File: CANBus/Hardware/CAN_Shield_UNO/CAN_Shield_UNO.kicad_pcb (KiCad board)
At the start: 2 copper layers, 68.6 x 53.3 mm, 39 parts, among them J1 Power, J2 Digital/PWM, J3 Analog, J4 Digital/PWM, J7 Screw_Terminal_01x02, U2 TCAN1051HGV

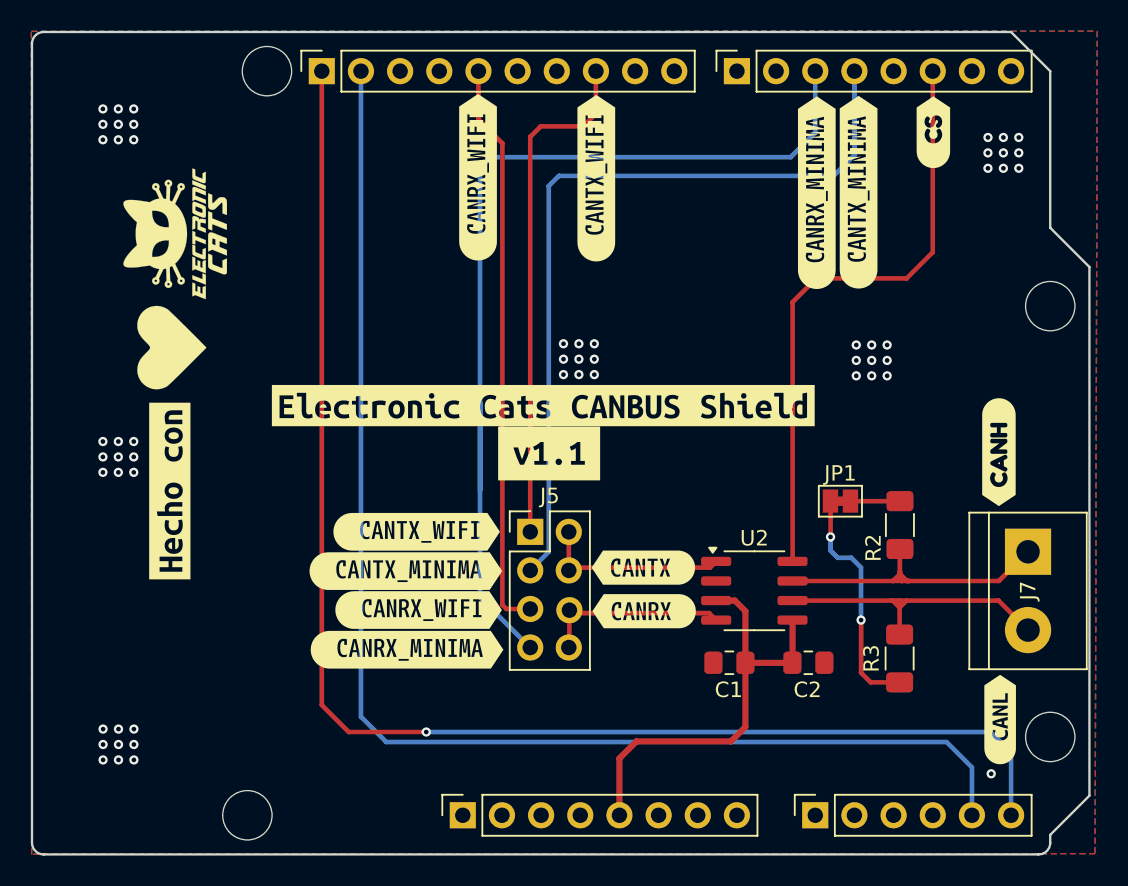
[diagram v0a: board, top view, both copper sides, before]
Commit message: feat(hw): to add hardware components
- Replacing the CAN Bus driver
- Adding a pull-down resistor to the CS pin
- Adding a 1nF capacitor to the 120 ohm terminating resistor
- Adding 2EDN7534F (54 Gate driver) channels to handle high current outputs; in addition adding a diode to power them if the board is only powered through USB
- Adding TL4050A50IDBZT (Precision micropower shunt voltage) to generate a precise 5V reference
- Adding protection diodes for A0 and A1 analog inputs
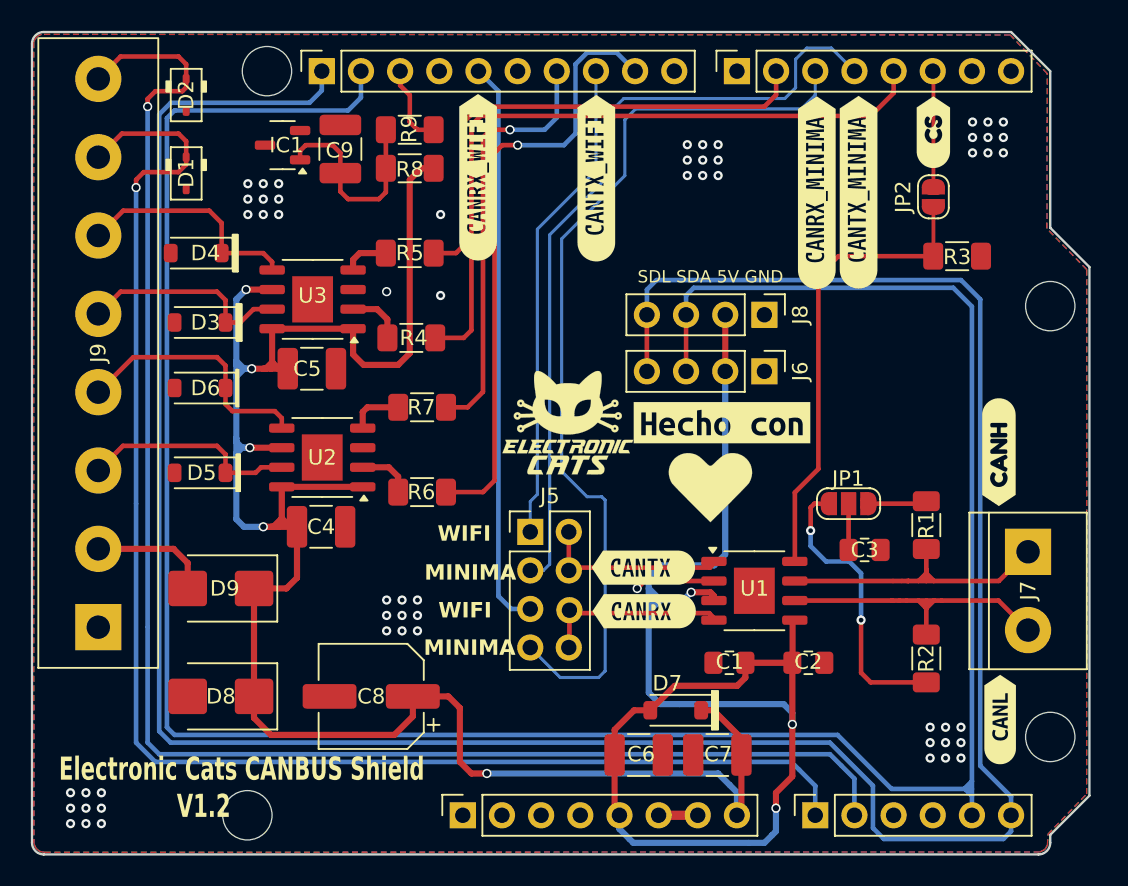
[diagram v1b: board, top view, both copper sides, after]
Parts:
- removed the kibuzzard-66182154 at (133.2, 70.9)
- removed kibuzzard-66182706: G***, kibuzzard-66182706
- removed kibuzzard-6618271B: G***, kibuzzard-6618271B
- removed kibuzzard-6618272A: G***, kibuzzard-6618272A
- removed kibuzzard-66182736: G***, kibuzzard-66182736
- removed kibuzzard-667B328E: G***, kibuzzard-667B328E
- removed kibuzzard-667B3298: G***, kibuzzard-667B3298
- added C3: 1000pF, Capacitor_SMD:C_0805_2012Metric_Pad1.18x1.45mm_HandSolder, F.Cu at (154.0, 80.2)
- added C4: 4.7uF, Capacitor_SMD:C_1210_3225Metric_Pad1.33x2.70mm_HandSolder, F.Cu at (118.8, 78.8)
- added C5: 4.7uF, Capacitor_SMD:C_1210_3225Metric_Pad1.33x2.70mm_HandSolder, F.Cu at (118.2, 68.5)
- added C6: 4.7uF, Capacitor_SMD:C_1210_3225Metric_Pad1.33x2.70mm_HandSolder, F.Cu at (139.3, 93.5)
- added C7: 4.7uF, Capacitor_SMD:C_1210_3225Metric_Pad1.33x2.70mm_HandSolder, F.Cu at (144.4, 93.5)
- added C8: 100uF, Capacitor_SMD:CP_Elec_6.3x7.7, F.Cu at (122.0, 89.8)
- added C9: 4,7uF, Capacitor_SMD:C_1210_3225Metric_Pad1.33x2.70mm_HandSolder, F.Cu at (120.0, 54.2)
- added D1: ESDA041-1JY, PCM_Diode_SMD_AKL:D_SOD-323, F.Cu at (110.0, 55.8)
- added D2: ESDA041-1JY, PCM_Diode_SMD_AKL:D_SOD-323, F.Cu at (110.0, 50.8)
- added D3: STPS1L40ZF, Diode_SMD:D_SOD-123, F.Cu at (110.9, 65.5)
- added D4: STPS1L40ZF, Diode_SMD:D_SOD-123, F.Cu at (110.7, 61.0)
- added D5: STPS1L40ZF, Diode_SMD:D_SOD-123, F.Cu at (110.9, 75.2)
- added D6: STPS1L40ZF, Diode_SMD:D_SOD-123, F.Cu at (110.9, 69.8)
- added D7: STPS1L40ZF, Diode_SMD:D_SOD-123, F.Cu at (141.8, 90.7)
- added D8: SMBJ16A, Diode_SMD:D_SMB, F.Cu at (112.2, 89.8)
- added D9: STPS3L40UF, Diode_SMD:D_SMB, F.Cu at (112.2, 82.8)
- added IC1: TL4050A50IDBZT, Package_TO_SOT_SMD:SOT-23-3, F.Cu at (116.2, 54.0)
- added J6: Grove connector, Connector_PinHeader_2.54mm:PinHeader_1x04_P2.54mm_Vertical, F.Cu at (147.5, 68.7)
- added J8: Grove connector, Connector_PinHeader_2.54mm:PinHeader_1x04_P2.54mm_Vertical, F.Cu at (147.5, 65.0)
- added J9: Screw_Terminal_01x08, TerminalBlock:TerminalBlock_bornier-8_P5.08mm, F.Cu at (104.3, 85.3)
- added JP2: SolderJumper, Jumper:SolderJumper-2_P1.3mm_Open_RoundedPad1.0x1.5mm, F.Cu at (158.5, 57.4)
- added R3: 10K, Resistor_SMD:R_1206_3216Metric_Pad1.30x1.75mm_HandSolder, F.Cu at (160.0, 61.2)
- added R4: 10K, Resistor_SMD:R_1206_3216Metric_Pad1.30x1.75mm_HandSolder, F.Cu at (124.6, 66.5)
- added R5: 10K, Resistor_SMD:R_1206_3216Metric_Pad1.30x1.75mm_HandSolder, F.Cu at (124.5, 61.0)
- added R6: 10K, Resistor_SMD:R_1206_3216Metric_Pad1.30x1.75mm_HandSolder, F.Cu at (125.3, 76.5)
- added R7: 10K, Resistor_SMD:R_1206_3216Metric_Pad1.30x1.75mm_HandSolder, F.Cu at (125.3, 71.0)
- added R8: 2K, Resistor_SMD:R_1206_3216Metric_Pad1.30x1.75mm_HandSolder, F.Cu at (124.5, 55.5)
- added R9: 22, Resistor_SMD:R_1206_3216Metric_Pad1.30x1.75mm_HandSolder, F.Cu at (124.5, 53.0)
- added U2: 2EDN7534F, Package_SO:Infineon_PG-DSO-8-27_3.9x4.9mm_EP2.65x3mm, F.Cu at (118.8, 74.3)
- added U3: 2EDN7534F, Package_SO:Infineon_PG-DSO-8-27_3.9x4.9mm_EP2.65x3mm, F.Cu at (118.2, 64.0)
- JP1: value SolderJumper_2_Bridged -> SolderJumper; footprint Jumper:SolderJumper-2_P1.3mm_Bridged_Pad1.0x1.5mm -> Jumper:SolderJumper-3_P1.3mm_Open_RoundedPad1.0x1.5mm_NumberLabels
- U1: renamed from U2; value TCAN1051HGV -> TLE9371VSJ; footprint Package_SO:SOIC-8_3.9x4.9mm_P1.27mm -> Package_SO:Infineon_PG-DSO-8-27_3.9x4.9mm_EP2.65x3mm
- moved kibuzzard-661820F9 36.1 mm to (144.8, 72.0), turned to 0 degrees
- moved Ref** 36.1 mm to (144.0, 76.2), turned to 180 degrees
- moved G*** 28.3 mm to (134.8, 72.0), turned to 0 degrees
- moved kibuzzard-66182154 21.7 mm to (156.2, 72.8), turned to -90 degrees
- moved G*** 10.2 mm to (118.5, 82.8)
- moved Ref** 9.97 mm to (118.2, 75.0)
- moved kibuzzard-661820F9 9.82 mm to (118.0, 65.5)
- moved R2 1.73 mm to (158.0, 87.3)
- moved R1 1.71 mm to (158.0, 78.6)
- moved JP1 0.55 mm to (153.0, 77.2)
- renumbered R2 to R1, R3 to R2
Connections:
- JP1 pad 2: Net-(JP1-B) -> Net-(JP1-C)
- U1 pad 8: /2 -> Net-(JP2-B)
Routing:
- net VCC: track 0.00 -> 133.5 mm, vias 0 -> 5
- net /A1: track 0.00 -> 101.7 mm, vias 0 -> 1
- net /A0: track 0.00 -> 95.3 mm, vias 0 -> 1
- net /SCL/A5: track 91.2 -> 175.4 mm, vias 1 -> 0
- net /SDA/A4: track 86.0 -> 166.7 mm
- net +5V: track 28.2 -> 92.6 mm, vias 0 -> 3
- net /*3: track 0.00 -> 45.5 mm
- net /*9: track 0.00 -> 39.7 mm, vias 0 -> 1
- net /*6: track 0.00 -> 32.2 mm
- net /2: track 39.0 -> 7.52 mm
- net Net-(JP2-B): track 0.00 -> 30.3 mm
- net /*11: track 0.00 -> 27.6 mm, vias 0 -> 1
- net /U4_Out2: track 0.00 -> 16.6 mm
- net /U5_Out2: track 0.00 -> 15.0 mm
- net /U4_Out1: track 0.00 -> 14.1 mm
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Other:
- board text added: "0,1uF"
- board text added: "60Ω"
- board text added: "A1 A0 11 9 6 3 +12 GND"
- board text added: "Electronic Cats CANBUS Shield V1.2"
- board text added: "MINIMA"
- board text added: "SDL SDA 5V GND"
- board text added: "WIFI"

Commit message: feat(Hw):Update_Route
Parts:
- moved C1 1.58 mm to (146.6, 86.8)
- moved C2 0.80 mm to (150.3, 86.8)
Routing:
- net +5V: track 92.6 -> 60.1 mm, vias 3 -> 2
- net GND: track 8.61 -> 1.56 mm, vias 58 -> 62
- net Net-(IC1-CATHODE): track 13.5 -> 8.82 mm
- net /CRX0_MINIMA: track 59.9 -> 61.0 mm
- net VCC: track 133.5 -> 134.5 mm
- net /*9: track 39.7 -> 40.2 mm
- net /SCL/A5: track 175.4 -> 176.0 mm

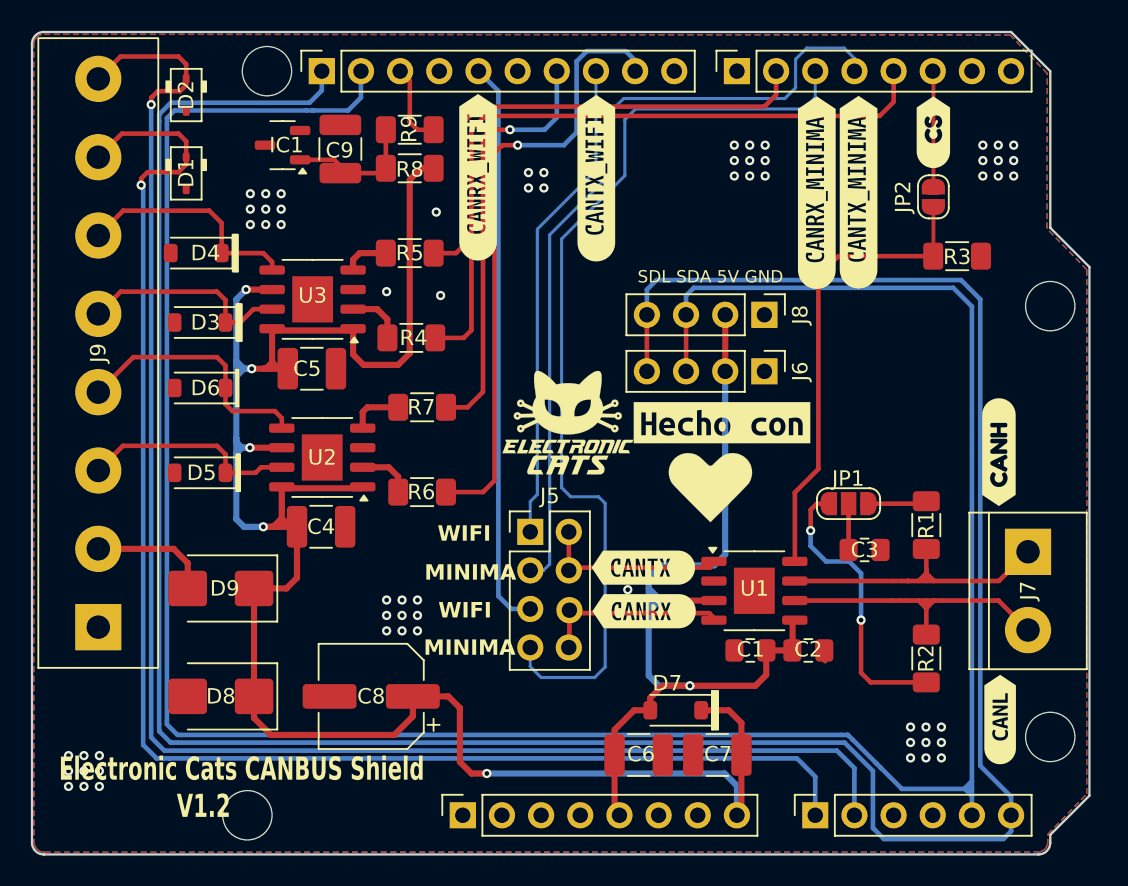
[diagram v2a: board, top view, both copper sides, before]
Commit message: feat(Hw):Update_Labels
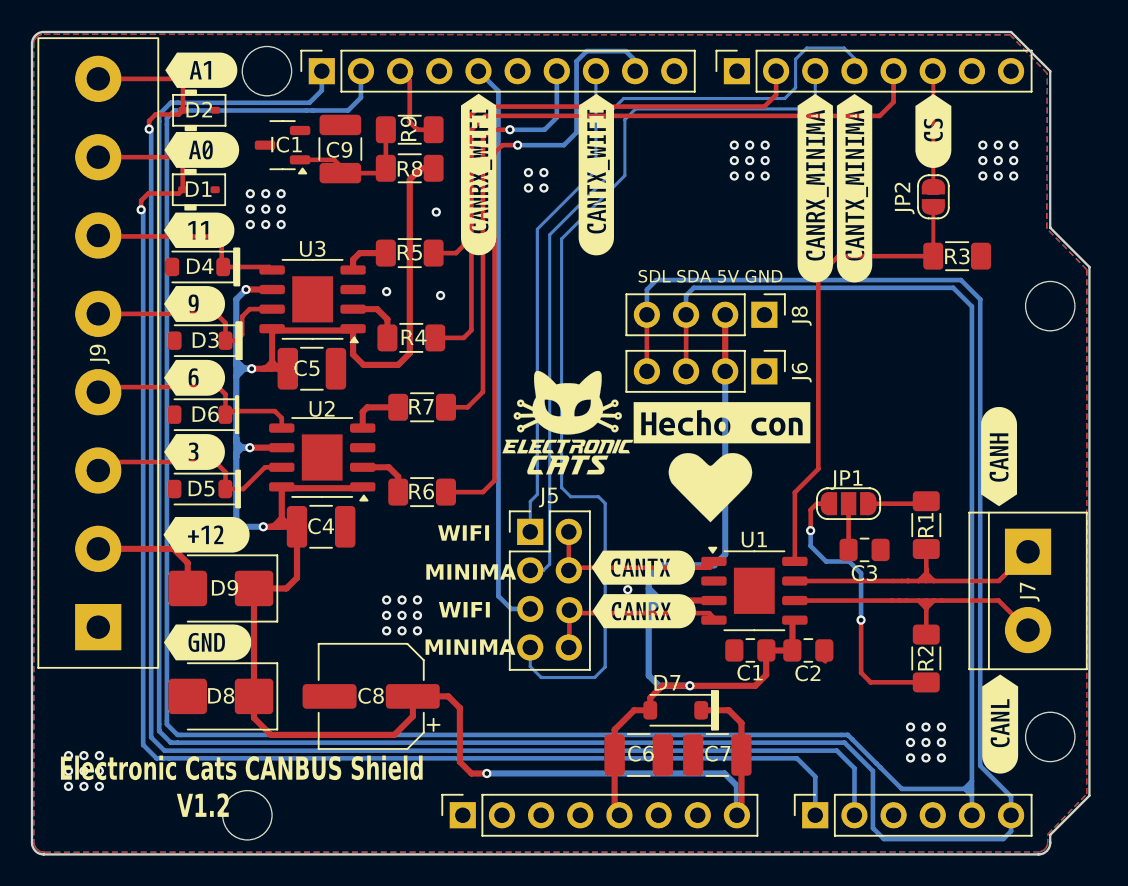
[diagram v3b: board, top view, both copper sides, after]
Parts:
- removed kibuzzard-66182422: G***, kibuzzard-66182422
- removed kibuzzard-66182455: G***, kibuzzard-66182455
- removed kibuzzard-6618247C: G***, kibuzzard-6618247C
- removed kibuzzard-66182965: G***, kibuzzard-66182965
- removed kibuzzard-66182980: G***, kibuzzard-66182980
- removed kibuzzard-661829B1: G***, kibuzzard-661829B1
- removed kibuzzard-661829C4: G***, kibuzzard-661829C4
- added REF**: OSHW-Logo_7.5x8mm_SilkScreen, Symbol:OSHW-Logo_7.5x8mm_SilkScreen, B.Cu at (134.6, 73.2)
- added kibuzzard-6810F491: G***, kibuzzard-6810F491, F.Cu at (136.6, 55.9)
- added kibuzzard-6810F519: G***, kibuzzard-6810F519, F.Cu at (129.0, 55.9)
- added kibuzzard-6810F55A: G***, kibuzzard-6810F55A, F.Cu at (150.8, 56.8)
- added kibuzzard-6810F58F: G***, kibuzzard-6810F58F, F.Cu at (153.3, 56.8)
- added kibuzzard-6810F647: G***, kibuzzard-6810F647, F.Cu at (158.5, 53.1)
- added kibuzzard-6810F6B3: G***, kibuzzard-6810F6B3, F.Cu at (162.8, 91.5)
- added kibuzzard-6810F7BA: G***, kibuzzard-6810F7BA, F.Cu at (162.7, 74.2)
- added kibuzzard-6810F7F0: G***, kibuzzard-6810F7F0, F.Cu at (111.4, 86.2)
- added kibuzzard-6810F82C: G***, kibuzzard-6810F82C, F.Cu at (111.3, 79.3)
- added kibuzzard-6810F8E2: G***, kibuzzard-6810F8E2, F.Cu at (110.5, 73.9)
- added kibuzzard-6810F93B: G***, kibuzzard-6810F93B, F.Cu at (110.5, 69.1)
- added kibuzzard-6810F9B1: G***, kibuzzard-6810F9B1, F.Cu at (110.5, 64.3)
- added kibuzzard-6810FD34: G***, kibuzzard-6810FD34, F.Cu at (110.8, 59.5)
- added kibuzzard-6810FDE2: G***, kibuzzard-6810FDE2, F.Cu at (111.0, 54.3)
- added kibuzzard-6810FE84: G***, kibuzzard-6810FE84, F.Cu at (111.0, 49.1)
- moved D6 1.73 mm to (110.9, 71.5)
- moved D1 1.35 mm to (110.8, 56.9), turned to 0 degrees
- moved D2 1.30 mm to (110.8, 51.7), turned to 0 degrees
- moved D3 1.18 mm to (110.9, 66.7)
- moved D5 1.05 mm to (110.9, 76.3)
- moved D4 0.91 mm to (110.8, 61.9)
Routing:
- net /A0: track 95.1 -> 92.6 mm
- net /A1: track 101.4 -> 99.2 mm
- net /U4_Out2: track 16.6 -> 14.5 mm
- net /U5_Out2: track 15.0 -> 13.0 mm
